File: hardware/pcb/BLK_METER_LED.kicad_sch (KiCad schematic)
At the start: 19 parts, among them J7 IDC-34 METER_LED, U5 ULN2803A, U6 74AHCT125, U7 74AHCT125, U8 ULN2803A, U9 MCP23017_ML

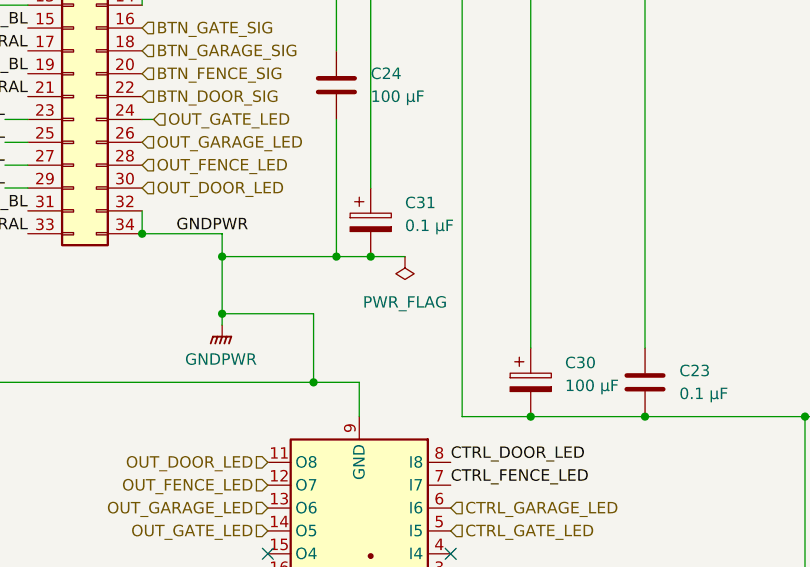
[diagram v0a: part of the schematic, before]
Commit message: Update hardware schematics and documentation; added source of truth for hardware, removed unused symbols, and modified connector specifications.
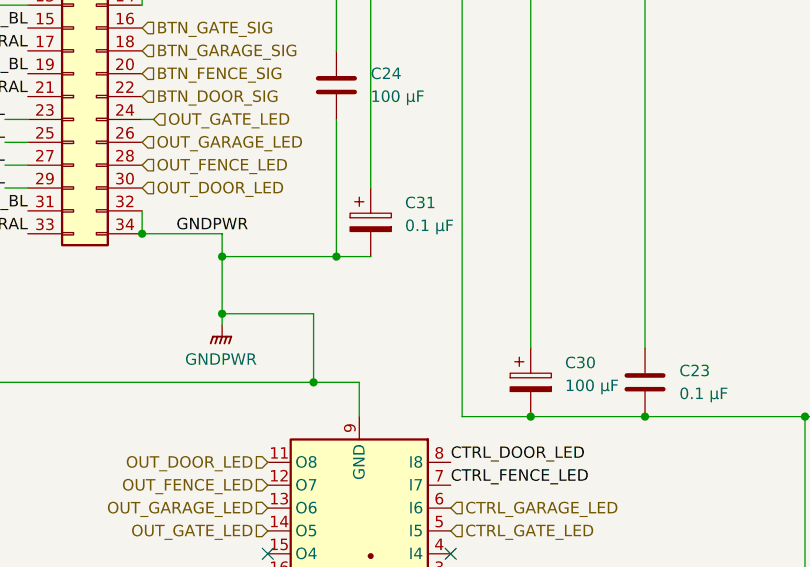
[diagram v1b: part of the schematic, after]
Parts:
- C24: footprint Capacitor_THT:C_Disc_D3.0mm_W1.6mm_P2.50mm -> Capacitor_THT:CP_Radial_D5.0mm_P2.50mm
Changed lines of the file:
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@@
 	)
 	(junction
-		(at 130.81 144.78)
-		(diameter 0)
-		(color 0 0 0 0)
-	)
-	(junction
 		(at 257.81 162.56)
 		(diameter 0)
@@
 	(wire
 		(pts
-			(xy 130.81 144.78) (xy 134.62 144.78)
-		)
-		(stroke
-			(width 0)
-			(type default)
-		)
-	)
-	(wire
-		(pts
 			(xy 90.17 208.28) (xy 90.17 204.47)
 		)
@@
 	)
 	(symbol
-		(lib_id "power:PWR_FLAG")
-		(at 134.62 144.78 180)
-		(unit 1)
-		(exclude_from_sim no)
-		(in_bom yes)
-		(on_board yes)
-		(dnp no)
-		(fields_autoplaced yes)
-		(property "Reference" "#FLG05"
-			(at 134.62 146.685 0)
-			(effects
-				(font
-					(size 1.27 1.27)
-				)
-				(hide yes)
-			)
-		)
-		(property "Value" "PWR_FLAG"
-			(at 134.62 149.86 0)
-			(effects
-				(font
-					(size 1.27 1.27)
-				)
-			)
-		)
-		(property "Footprint" ""
-			(at 134.62 144.78 0)
-			(effects
-				(font
-					(size 1.27 1.27)
-				)
-				(hide yes)
-			)
-		)
-		(property "Datasheet" "~"
-			(at 134.62 144.78 0)
-			(effects
-				(font
-					(size 1.27 1.27)
-				)
-				(hide yes)
-			)
-		)
-		(property "Description" "Special symbol for telling ERC where power comes from"
-			(at 134.62 144.78 0)
-			(effects
-				(font
-					(size 1.27 1.27)
-				)
-				(hide yes)
-			)
-		)
-		(pin "1"
-		)
-		(instances
-			(project "powerplant"
-				(path "/466a31f8-107b-4c4c-9290-aff37fe81c1e/db7adffd-aa7d-4a46-a5c7-199e9f0c5b1e"
-					(reference "#FLG05")
-					(unit 1)
-				)
-			)
-		)
-	)
-	(symbol
 		(lib_id "74xx:74AHCT125")
 		(at 226.06 64.77 180)
@@
 			)
 		)
-		(property "Footprint" "Capacitor_THT:C_Disc_D3.0mm_W1.6mm_P2.50mm"
+		(property "Footprint" "Capacitor_THT:CP_Radial_D5.0mm_P2.50mm"
 			(at 126.0348 121.92 0)
 			(effects
